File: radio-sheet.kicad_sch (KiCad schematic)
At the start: 46 parts, among them Q2 AO3401A, Q3 MMBT3904, Q4 AO3401A, U15 74HC04, U5 Si4463, Y4 30M

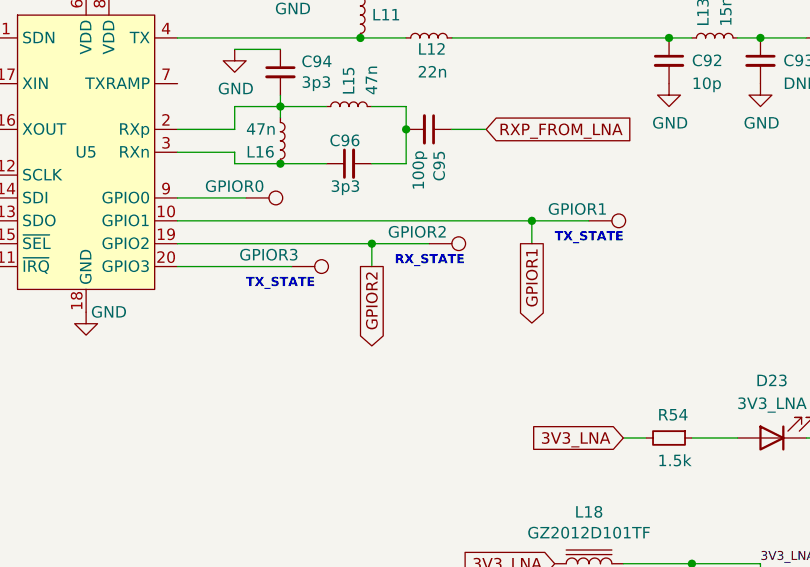
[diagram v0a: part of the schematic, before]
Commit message: RX and TX leds together, minor layout & silk fixes etc
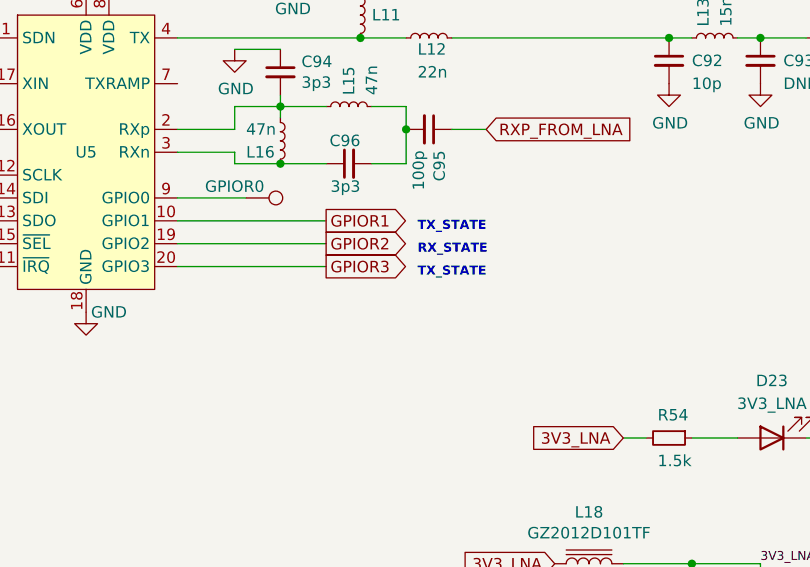
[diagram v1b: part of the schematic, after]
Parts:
- removed GPIOR1, GPIOR2, GPIOR3: TestPoint, TestPoint:TestPoint_Pad_D1.5mm, symbol Connector:TestPoint
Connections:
- net GPIOR3: now reaches U5.20 (GPIO3)
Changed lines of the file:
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@@
   (junction (at 189.23 52.07) (diameter 0) (color 0 0 0 0)
   )
-  (junction (at 156.21 74.93) (diameter 0) (color 0 0 0 0)
-  )
   (junction (at 91.44 95.25) (diameter 0) (color 0 0 0 0)
   )
@@
   (junction (at 191.77 110.49) (diameter 0) (color 0 0 0 0)
   )
-  (junction (at 173.99 72.39) (diameter 0) (color 0 0 0 0)
-  )
   (junction (at 124.46 40.64) (diameter 0) (color 0 0 0 0)
   )
@@
     (stroke (width 0) (type default) (color 0 0 0 0))
   )
-  (wire (pts (xy 173.99 72.39) (xy 180.34 72.39))
-    (stroke (width 0) (type default) (color 0 0 0 0))
-  )
   (wire (pts (xy 91.44 130.81) (xy 91.44 128.27))
     (stroke (width 0) (type default) (color 0 0 0 0))
@@
     (stroke (width 0) (type default) (color 0 0 0 0))
   )
-  (wire (pts (xy 173.99 74.93) (xy 173.99 72.39))
-    (stroke (width 0) (type default) (color 0 0 0 0))
-  )
   (wire (pts (xy 154.94 41.91) (xy 154.94 39.37))
     (stroke (width 0) (type default) (color 0 0 0 0))
@@
     (stroke (width 0) (type default) (color 0 0 0 0))
   )
-  (wire (pts (xy 134.62 72.39) (xy 173.99 72.39))
-    (stroke (width 0) (type default) (color 0 0 0 0))
-  )
   (wire (pts (xy 146.05 66.04) (xy 151.13 66.04))
     (stroke (width 0) (type default) (color 0 0 0 0))
   )
-  (wire (pts (xy 156.21 74.93) (xy 162.56 74.93))
-    (stroke (width 0) (type default) (color 0 0 0 0))
-  )
   (wire (pts (xy 114.3 128.27) (xy 114.3 121.92))
     (stroke (width 0) (type default) (color 0 0 0 0))
@@
     (stroke (width 0) (type default) (color 0 0 0 0))
   )
-  (wire (pts (xy 134.62 74.93) (xy 156.21 74.93))
-    (stroke (width 0) (type default) (color 0 0 0 0))
-  )
   (wire (pts (xy 127 45.72) (xy 127 46.99))
     (stroke (width 0) (type default) (color 0 0 0 0))
@@
     (stroke (width 0) (type default) (color 0 0 0 0))
   )
-  (wire (pts (xy 134.62 77.47) (xy 147.32 77.47))
-    (stroke (width 0) (type default) (color 0 0 0 0))
-  )
-  (wire (pts (xy 156.21 77.47) (xy 156.21 74.93))
+  (wire (pts (xy 134.62 77.47) (xy 151.13 77.47))
+    (stroke (width 0) (type default) (color 0 0 0 0))
+  )
+  (wire (pts (xy 134.62 74.93) (xy 151.13 74.93))
     (stroke (width 0) (type default) (color 0 0 0 0))
   )
@@
   )
   (wire (pts (xy 185.42 27.94) (xy 173.99 27.94))
+    (stroke (width 0) (type default) (color 0 0 0 0))
+  )
+  (wire (pts (xy 134.62 72.39) (xy 151.13 72.39))
     (stroke (width 0) (type default) (color 0 0 0 0))
   )
@@
     (effects (font (size 3.9878 3.9878) (thickness 0.7976) bold italic) (justify left bottom))
   )
-  (text "RX_STATE" (at 158.75 77.47 0)
+  (text "RX_STATE" (at 161.29 76.2 0)
     (effects (font (size 1.016 1.016) (thickness 0.2032) bold) (justify left bottom))
   )
@@
     (effects (font (size 2.0066 2.0066) (thickness 0.4013) bold italic) (justify left bottom))
   )
-  (text "TX_STATE" (at 142.24 80.01 0)
+  (text "TX_STATE" (at 161.29 78.74 0)
     (effects (font (size 1.016 1.016) (thickness 0.2032) bold) (justify left bottom))
   )
@@
     (effects (font (size 2.0066 2.0066) (thickness 0.4013) bold) (justify right bottom))
   )
-  (text "TX_STATE" (at 176.53 74.93 0)
+  (text "TX_STATE" (at 161.29 73.66 0)
     (effects (font (size 1.016 1.016) (thickness 0.2032) bold) (justify left bottom))
   )
@@
     )
   )
-  (global_label "GPIOR1" (shape output) (at 173.99 74.93 270) (fields_autoplaced)
-    (effects (font (size 1.27 1.27)) (justify right))
-    (property "Intersheet References" "${INTERSHEET_REFS}" (id 0) (at 0 0 0)
+  (global_label "GPIOR1" (shape output) (at 151.13 72.39 0) (fields_autoplaced)
+    (effects (font (size 1.27 1.27)) (justify left))
+    (property "Intersheet References" "${INTERSHEET_REFS}" (id 0) (at 76.2 246.38 0)
       (effects (font (size 1.27 1.27)) hide)
     )
@@
     )
   )
+  (global_label "GPIOR3" (shape output) (at 151.13 77.47 0) (fields_autoplaced)
+    (effects (font (size 1.27 1.27)) (justify left))
+    (property "Intersheet References" "${INTERSHEET_REFS}" (id 0) (at 160.409 77.3906 0)
+      (effects (font (size 1.27 1.27)) (justify left) hide)
+    )
+  )
   (global_label "SWDC_PA_TX_12V" (shape input) (at 114.3 128.27 180) (fields_autoplaced)
     (effects (font (size 1.27 1.27)) (justify right))
@@
     )
   )
-  (global_label "GPIOR2" (shape output) (at 156.21 77.47 270) (fields_autoplaced)
-    (effects (font (size 1.27 1.27)) (justify right))
-    (property "Intersheet References" "${INTERSHEET_REFS}" (id 0) (at 0 0 0)
+  (global_label "GPIOR2" (shape output) (at 151.13 74.93 0) (fields_autoplaced)
+    (effects (font (size 1.27 1.27)) (justify left))
+    (property "Intersheet References" "${INTERSHEET_REFS}" (id 0) (at 73.66 231.14 0)
       (effects (font (size 1.27 1.27)) hide)
     )
@@
       (effects (font (size 1.27 1.27)) hide)
     )
-    (pin "1")
-  )
-  (symbol (lib_id "Connector:TestPoint") (at 180.34 72.39 270) (unit 1)
-    (in_bom yes) (on_board yes)
-    (property "Reference" "GPIOR1" (id 0) (at 179.07 71.12 90))
-    (property "Value" "TestPoint" (id 1) (at 190.5 72.39 90)
-      (effects (font (size 1.27 1.27)) hide)
-    )
-    (property "Footprint" "TestPoint:TestPoint_Pad_D1.5mm" (id 2) (at 180.34 77.47 0)
-      (effects (font (size 1.27 1.27)) hide)
-    )
-    (property "Datasheet" "~" (id 3) (at 180.34 77.47 0)
-      (effects (font (size 1.27 1.27)) hide)
-    )
-    (property "DNP" "TRUE" (id 4) (at 180.34 72.39 0)
-      (effects (font (size 1.27 1.27)) hide)
-    )
-    (pin "1")
-  )
-  (symbol (lib_id "Connector:TestPoint") (at 162.56 74.93 270) (unit 1)
-    (in_bom yes) (on_board yes)
-    (property "Reference" "GPIOR2" (id 0) (at 161.29 73.66 90))
-    (property "Value" "TestPoint" (id 1) (at 172.72 74.93 90)
-      (effects (font (size 1.27 1.27)) hide)
-    )
-    (property "Footprint" "TestPoint:TestPoint_Pad_D1.5mm" (id 2) (at 162.56 80.01 0)
-      (effects (font (size 1.27 1.27)) hide)
-    )
-    (property "Datasheet" "~" (id 3) (at 162.56 80.01 0)
-      (effects (font (size 1.27 1.27)) hide)
-    )
-    (property "DNP" "TRUE" (id 4) (at 162.56 74.93 0)
-      (effects (font (size 1.27 1.27)) hide)
-    )
-    (pin "1")
-  )
-  (symbol (lib_id "Connector:TestPoint") (at 147.32 77.47 270) (unit 1)
-    (in_bom yes) (on_board yes)
-    (property "Reference" "GPIOR3" (id 0) (at 144.78 76.2 90))
-    (property "Value" "TestPoint" (id 1) (at 157.48 77.47 90)
-      (effects (font (size 1.27 1.27)) hide)
-    )
-    (property "Footprint" "TestPoint:TestPoint_Pad_D1.5mm" (id 2) (at 147.32 82.55 0)
-      (effects (font (size 1.27 1.27)) hide)
-    )
-    (property "Datasheet" "~" (id 3) (at 147.32 82.55 0)
-      (effects (font (size 1.27 1.27)) hide)
-    )
-    (property "DNP" "TRUE" (id 4) (at 147.32 77.47 0)
-      (effects (font (size 1.27 1.27)) hide)
-    )

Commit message: misc
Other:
- moved on the sheet: D23, R54

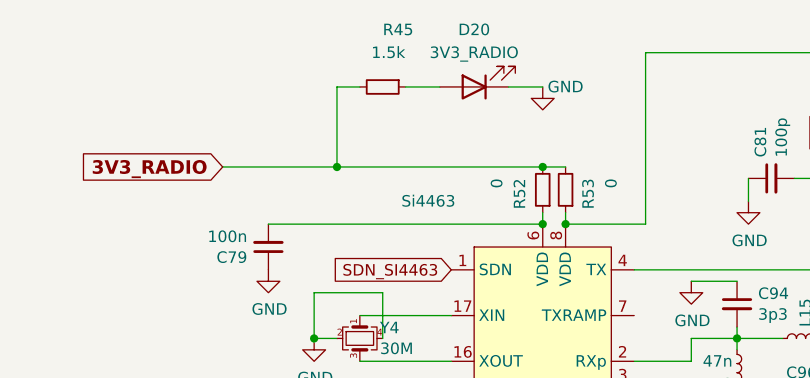
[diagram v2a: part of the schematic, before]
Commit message: lots of silkscreen enhancements
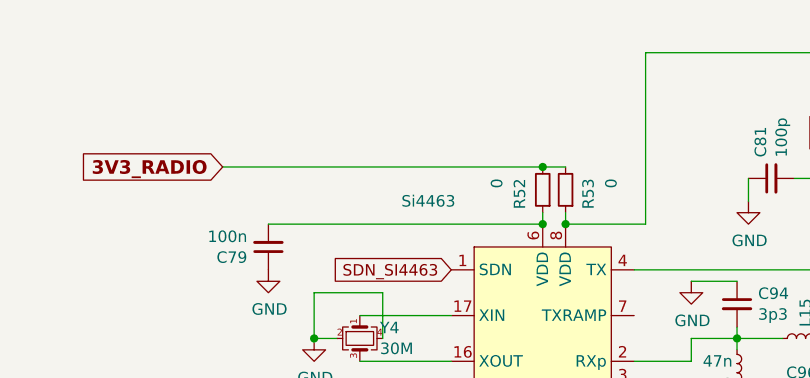
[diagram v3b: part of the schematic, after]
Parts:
- removed D20: 3V3_RADIO, LED_SMD:LED_0603_1608Metric, symbol Device:LED
- removed R45: 1.5k, Resistor_SMD:R_0603_1608Metric, symbol Device:R_Small
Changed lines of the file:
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@@
   (junction (at 246.38 109.22) (diameter 0) (color 0 0 0 0)
   )
-  (junction (at 101.6 40.64) (diameter 0) (color 0 0 0 0)
-  )
   (junction (at 189.23 52.07) (diameter 0) (color 0 0 0 0)
   )
@@
     (stroke (width 0) (type default) (color 0 0 0 0))
   )
-  (wire (pts (xy 101.6 31.75) (xy 101.6 40.64))
-    (stroke (width 0) (type default) (color 0 0 0 0))
-  )
   (wire (pts (xy 124.46 40.64) (xy 127 40.64))
     (stroke (width 0) (type default) (color 0 0 0 0))
@@
     (stroke (width 0) (type default) (color 0 0 0 0))
   )
-  (wire (pts (xy 101.6 31.75) (xy 104.14 31.75))
-    (stroke (width 0) (type default) (color 0 0 0 0))
-  )
   (wire (pts (xy 165.1 62.23) (xy 168.91 62.23))
     (stroke (width 0) (type default) (color 0 0 0 0))
@@
     (stroke (width 0) (type default) (color 0 0 0 0))
   )
-  (wire (pts (xy 88.9 40.64) (xy 101.6 40.64))
-    (stroke (width 0) (type default) (color 0 0 0 0))
-  )
   (wire (pts (xy 93.98 46.99) (xy 124.46 46.99))
     (stroke (width 0) (type default) (color 0 0 0 0))
@@
     (stroke (width 0) (type default) (color 0 0 0 0))
   )
-  (wire (pts (xy 109.22 31.75) (xy 113.03 31.75))
-    (stroke (width 0) (type default) (color 0 0 0 0))
-  )
   (wire (pts (xy 199.39 135.89) (xy 194.31 135.89))
     (stroke (width 0) (type default) (color 0 0 0 0))
@@
     (stroke (width 0) (type default) (color 0 0 0 0))
   )
-  (wire (pts (xy 101.6 40.64) (xy 124.46 40.64))
+  (wire (pts (xy 88.9 40.64) (xy 124.46 40.64))
     (stroke (width 0) (type default) (color 0 0 0 0))
   )
@@
   )
   (wire (pts (xy 135.89 46.99) (xy 127 46.99))
-    (stroke (width 0) (type default) (color 0 0 0 0))
-  )
-  (wire (pts (xy 120.65 31.75) (xy 124.46 31.75))
     (stroke (width 0) (type default) (color 0 0 0 0))
   )
@@
     (pin "2")
   )
-  (symbol (lib_id "Device:LED") (at 116.84 31.75 180) (unit 1)
-    (in_bom yes) (on_board yes)
-    (property "Reference" "D20" (id 0) (at 116.84 25.4 0))
-    (property "Value" "3V3_RADIO" (id 1) (at 116.84 27.94 0))
-    (property "Footprint" "LED_SMD:LED_0603_1608Metric" (id 2) (at 116.84 31.75 0)
-      (effects (font (size 1.27 1.27)) hide)
-    )
-    (property "Datasheet" "~" (id 3) (at 116.84 31.75 0)
-      (effects (font (size 1.27 1.27)) hide)
-    )
-    (property "LCSC" "C72043" (id 4) (at 116.84 31.75 0)
-      (effects (font (size 1.27 1.27)) hide)
-    )
-    (pin "1")
-    (pin "2")
-  )
-  (symbol (lib_id "Device:R_Small") (at 106.68 31.75 270) (unit 1)
-    (in_bom yes) (on_board yes)
-    (property "Reference" "R45" (id 0) (at 106.68 25.4 90)
-      (effects (font (size 1.27 1.27)) (justify left))
-    )
-    (property "Value" "1.5k" (id 1) (at 105.41 27.94 90)
-      (effects (font (size 1.27 1.27)) (justify left))
-    )
-    (property "Footprint" "Resistor_SMD:R_0603_1608Metric" (id 2) (at 106.68 31.75 0)
-      (effects (font (size 1.27 1.27)) hide)
-    )
-    (property "Datasheet" "~" (id 3) (at 106.68 31.75 0)
-      (effects (font (size 1.27 1.27)) hide)
-    )
-    (property "LCSC" "C22843" (id 4) (at 106.68 31.75 0)
-      (effects (font (size 1.27 1.27)) hide)
-    )
-    (pin "1")
-    (pin "2")
-  )
-  (symbol (lib_id "power:GND") (at 124.46 31.75 0) (unit 1)
-    (in_bom yes) (on_board yes)
-    (property "Reference" "#PWR0170" (id 0) (at 124.46 38.1 0)
-      (effects (font (size 1.27 1.27)) hide)
-    )
-    (property "Value" "GND" (id 1) (at 127 31.75 0))
-    (property "Footprint" "" (id 2) (at 124.46 31.75 0)
-      (effects (font (size 1.27 1.27)) hide)
-    )
-    (property "Datasheet" "" (id 3) (at 124.46 31.75 0)
-      (effects (font (size 1.27 1.27)) hide)
-    )
-    (pin "1")
-  )
   (symbol (lib_id "74xx:74HC04") (at 93.98 165.1 0) (unit 1)

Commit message: replaced out-of-stock components LCSC codes with new ones
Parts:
- R38, R49, R54: LCSC C22843 -> C118397
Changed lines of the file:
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@@
       (effects (font (size 1.27 1.27)) hide)
     )
-    (property "LCSC" "C22843" (id 4) (at 68.58 134.62 0)
+    (property "LCSC" "C118397" (id 4) (at 68.58 134.62 0)
       (effects (font (size 1.27 1.27)) hide)
     )
@@
       (effects (font (size 1.27 1.27)) hide)
     )
-    (property "LCSC" "C22843" (id 4) (at 31.75 116.84 0)
+    (property "LCSC" "C118397" (id 4) (at 31.75 116.84 0)
       (effects (font (size 1.27 1.27)) hide)
     )
@@
       (effects (font (size 1.27 1.27)) hide)
     )
-    (property "LCSC" "C22843" (id 4) (at 180.34 95.25 0)
-      (effects (font (size 1.27 1.27)) hide)
-    )
+    (property "LCSC" "C118397" (id 4) (at 180.34 95.25 0)
+      (effects (font (size 1.27 1.27)) hide)
+    )

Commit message: LCSC codes changed (out-of-stock parts)
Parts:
- Y4: LCSC C251625 -> C2149121
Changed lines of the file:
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@@
       (effects (font (size 1.27 1.27)) hide)
     )
-    (property "LCSC" "C251625" (id 4) (at 104.14 59.69 0)
+    (property "LCSC" "C2149121" (id 4) (at 104.14 59.69 0)
       (effects (font (size 1.27 1.27)) hide)
     )
